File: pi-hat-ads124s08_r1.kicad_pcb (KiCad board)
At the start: 4 copper layers, 65 x 56 mm, 65 parts, among them J1 GPIO, J2 Conn_01x06, J3 Conn_01x06, J4 Conn_01x06, J5 Conn_01x06, J6 Conn_01x04, J7 Conn_01x02, Q1 S8550, U1 M24c64, U2 HX711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

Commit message: blocking out...
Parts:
- removed C2: 100nF, Capacitor_SMD:C_0603_1608Metric
- removed Q1: S8550, Package_TO_SOT_SMD:SOT-23
- removed R11, R13: 10k, Resistor_SMD:R_0603_1608Metric
- removed R12, R15, R20: 0R, Resistor_SMD:R_0603_1608Metric
- removed R14: 3k9, Resistor_SMD:R_0603_1608Metric
- removed R16, R17: 100R, Resistor_SMD:R_0603_1608Metric
- removed TP1: TestPoint, TestPoint:TestPoint_THTPad_2.0x2.0mm_Drill1.0mm
- added C17: 10nF, Capacitor_SMD:C_0603_1608Metric, F.Cu at (119.6, 80.7)
- C3: value 10uF -> 100nF; footprint Capacitor_SMD:C_0805_2012Metric -> Capacitor_SMD:C_0603_1608Metric
- C4: value 100nF -> 1uF
- C5: value 100nF -> 220nF
- C9: value 33pF -> 220nF
- J6: value Conn_01x04 -> Conn_01x06; footprint Connector_PinHeader_2.54mm:PinHeader_1x04_P2.54mm_Vertical -> Connector_PinHeader_2.54mm:PinHeader_1x06_P2.54mm_Vertical
- R10, R9: value 0R -> 1k
- R2, R4: value 100R -> 10k
- U2: value HX711 -> ADS124S08; footprint Package_SO:SOIC-16_3.9x9.9mm_P1.27mm -> Package_QFP:TQFP-32_5x5mm_P0.5mm
- moved J7 55.8 mm to (161.0, 71.9), turned to 90 degrees
- moved R9 23.9 mm to (146.5, 83.7), turned to 90 degrees
- moved R10 23.2 mm to (144.0, 83.8), turned to 90 degrees
- moved J4 23.0 mm to (135.8, 96.6), turned to 0 degrees
- moved R8 22.2 mm to (145.8, 56.0), turned to -90 degrees
- moved J6 19.7 mm to (132.2, 38.2), turned to 180 degrees
- moved C9 19.4 mm to (123.0, 73.0), turned to -90 degrees
- moved D2 18.0 mm to (155.8, 87.2), turned to 0 degrees
- moved C3 14.7 mm to (135.8, 71.7)
- moved J3 13.3 mm to (151.6, 87.2), turned to -90 degrees
- moved R4 11.4 mm to (118.1, 83.5), turned to 90 degrees
- moved D3 11.3 mm to (130.2, 87.2)
- moved J5 11.3 mm to (125.9, 87.2)
- moved J2 11.2 mm to (110.1, 96.6)
- moved R2 11.2 mm to (120.8, 83.5), turned to 90 degrees
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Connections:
- C3 pad 1: /EXE1+ -> +3V3
- C4 pad 1: /EXE1+ -> Net-(U2C-REFOUT)
- C5 pad 1: Net-(U2-VBG) -> VDDA
- C9 pad 1: Net-(U2-XI) -> VDDA
- C9 pad 2: /GPIO13/PWM1 -> GND
- D2 pad 2: GND -> /EXE1-
- D3 pad 1: /EXE1+ -> /EXE2+
- D3 pad 2: GND -> /EXE2-
- J2 pad 1: GND -> /EXE1-
- J3 pad 1: /EXE1+ -> /EXE2+
- J3 pad 6: GND -> /EXE2-
- J4 pad 1: GND -> /EXE2-
- J4 pad 6: /EXE1+ -> /EXE2+
- J5 pad 6: GND -> /EXE1-
- J6 pad 1: /GPIO8/SPI0.CE0 -> unconnected-(J6-Pin_1-Pad1)
- J6 pad 2: /GPIO9/SPI0.MISO -> /GPIO10/SPI0.MOSI
- J6 pad 4: /GPIO13/PWM1 -> /GPIO9/SPI0.MISO
- R10 pad 1: /EXE1+ -> /BR_OUT2-
- R10 pad 2: Net-(Q1-E) -> /Analog/INB-
- R2 pad 1: /Analog/IN1+ -> /BR_OUT1+
- R2 pad 2: /BR_OUT1+ -> /Analog/INA+
- R4 pad 1: /Analog/IN1- -> /BR_OUT1-
- R4 pad 2: /BR_OUT1- -> /Analog/INA-
- R8 pad 1: Net-(Q1-B) -> GND
- R8 pad 2: Net-(U2-BASE) -> /GPIO13/PWM1
- R9 pad 1: Net-(Q1-E) -> /BR_OUT2+
- R9 pad 2: VDDA -> /Analog/INB+
- U2 pad 1: VDDA -> unconnected-(U2A-AINCOM-Pad1)
- U2 pad 10: /Analog/INB+ -> /GPIO10/SPI0.MOSI
- U2 pad 13: unconnected-(U2-XO-Pad13) -> /GPIO17
- U2 pad 14: Net-(U2-XI) -> GND
- U2 pad 15: Net-(U2-RATE) -> +3V3
- U2 pad 2: Net-(U2-BASE) -> unconnected-(U2A-AIN5-Pad2)
- U2 pad 3: /EXE1+ -> unconnected-(U2A-AIN4-Pad3)
- U2 pad 4: Net-(U2-VFB) -> /Analog/INA-
- U2 pad 5: GND -> /Analog/INA+
- U2 pad 6: Net-(U2-VBG) -> /Analog/INB-
- U2 pad 7: /Analog/IN1- -> /Analog/INB+
- U2 pad 8: /Analog/IN1+ -> /GPIO5
- U2 pad 9: /Analog/INB- -> /GPIO8/SPI0.CE0
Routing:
- net /EXE1+: track 108.2 -> 21.0 mm, vias 5 -> 0
- net /GPIO10/SPI0.MOSI: track 0.00 -> 37.1 mm
- net +5V: track 70.9 -> 46.7 mm
- net +3V3: track 66.3 -> 47.5 mm, vias 3 -> 2
- net /GPIO8/SPI0.CE0: track 28.7 -> 45.0 mm
- net /power/VBOOST: track 39.8 -> 24.4 mm
- net /GPIO13/PWM1: track 23.5 -> 10.6 mm, vias 1 -> 0
- net Net-(U2-VFB): track 11.0 -> 0.00 mm
- net /GPIO11/SPI0.SCLK: track 38.5 -> 29.3 mm
- net /Analog/IN1-: track 8.66 -> 0.00 mm
- net VDDA: track 27.1 -> 18.9 mm
- net Net-(U2-VBG): track 7.76 -> 0.00 mm
- net /BR_OUT2-: track 16.3 -> 8.87 mm
- net /BR_OUT2+: track 16.0 -> 9.08 mm
- net Net-(U2-XI): track 6.70 -> 0.00 mm
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- removed copper zone on F.Cu, net /EXE1+
- removed copper zone on In2.Cu, net /EXE1+
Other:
- outline, holes or cut-outs redrawn
- board text removed: "CAMERA (OPTIONAL)"
- board text removed: "EX+"
- board text removed: "VDDA Mode R8<->R10 R20<->R15"

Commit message: progressing, blocking things out, pondering orbz
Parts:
- moved J6 27.9 mm to (136.4, 65.8), turned to 90 degrees
- moved R8 14.0 mm to (133.3, 62.4), turned to 90 degrees
- moved C10 1.00 mm to (145.2, 82.0)
- moved C17 1.00 mm to (119.6, 81.7)
- moved D2 1.00 mm to (155.8, 88.2)
- moved D3 1.00 mm to (130.2, 88.2)
- moved J3 1.00 mm to (151.6, 88.2)
- moved J5 1.00 mm to (125.9, 88.2)
- moved R10 1.00 mm to (144.0, 84.8)
- moved R2 1.00 mm to (120.8, 84.5)
- moved R4 1.00 mm to (118.1, 84.5)
- moved R9 1.00 mm to (146.5, 84.7)
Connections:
- J6 pad 1: unconnected-(J6-Pin_1-Pad1) -> /GPIO24
- J6 pad 2: /GPIO10/SPI0.MOSI -> /GPIO9/SPI0.MISO
- J6 pad 4: /GPIO9/SPI0.MISO -> /GPIO10/SPI0.MOSI
- J6 pad 6: unconnected-(J6-Pin_6-Pad6) -> /GPIO5
- R8 pad 2: /GPIO13/PWM1 -> /GPIO18/PCM.CLK
- U2 pad 13: /GPIO17 -> /GPIO24
- U2 pad 17: /GPIO13/PWM1 -> /GPIO18/PCM.CLK
- U2 pad 18: /GPIO6 -> /GPIO22
- U2 pad 2: unconnected-(U2A-AIN5-Pad2) -> /Analog/INA-
- U2 pad 3: unconnected-(U2A-AIN4-Pad3) -> /Analog/INA+
- U2 pad 4: /Analog/INA- -> unconnected-(U2A-AIN3-Pad4)
- U2 pad 5: /Analog/INA+ -> unconnected-(U2A-AIN2-Pad5)
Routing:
- net /GPIO5: track 0.00 -> 44.6 mm
- net /GPIO24: track 0.00 -> 36.1 mm
- net /GPIO18/PCM.CLK: track 0.00 -> 31.9 mm, vias 0 -> 1
- net /REFIN2+: track 7.60 -> 36.2 mm, vias 0 -> 1
- net /GPIO22: track 0.00 -> 25.5 mm, vias 0 -> 1
- net /REFIN2-: track 7.58 -> 30.9 mm, vias 0 -> 1
- net +5V: track 46.7 -> 23.9 mm
- net /REFIN1-: track 10.2 -> 30.8 mm
- net /REFIN1+: track 10.3 -> 27.7 mm, vias 0 -> 1
- net /Analog/INB+: track 0.00 -> 16.4 mm
- net /Analog/INB-: track 0.00 -> 15.7 mm
- net /Analog/INA-: track 0.00 -> 11.8 mm
- net /Analog/INA+: track 0.00 -> 11.0 mm
- net /GPIO13/PWM1: track 10.6 -> 0.00 mm
- net /GPIO9/SPI0.MISO: track 41.5 -> 32.7 mm
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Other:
- board text added: "ADS124S08-IIO-Eval karlp@tweak.au rev2025.10"
- board text added: "DRDY MISO CLK MOSI START"
- board text removed: "HX711-IIO-Eval karlp@tweak.au rev2025.09"
- board text removed: "Rate DO CLK XI"

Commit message: overhausl inputs a lot
read too much, thought too much.
try one with the "just 0R plus a nice big good quality cap" from the TI
precision seminar, describing common realities, as well as mixing in
what they did on the ads1262ref scale design document for the second
channel with a more "full blown" input filter.

I don't really like how none of this seems to be a proper AA filter,
but... ok.
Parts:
- added R11: 22R, Resistor_SMD:R_0603_1608Metric, F.Cu at (163.4, 103.7)
- added R12: 22R, Resistor_SMD:R_0603_1608Metric, F.Cu at (160.8, 103.7)
- added R13: 22R, Resistor_SMD:R_0603_1608Metric, F.Cu at (158.3, 103.7)
- added R14: 22R, Resistor_SMD:R_0603_1608Metric, F.Cu at (155.8, 103.7)
- added R15: 22R, Resistor_SMD:R_0603_1608Metric, F.Cu at (153.3, 103.7)
- added R16: 22R, Resistor_SMD:R_0603_1608Metric, F.Cu at (150.8, 103.7)
- added R17: 22R, Resistor_SMD:R_0603_1608Metric, F.Cu at (148.3, 103.7)
- added REF**: R_Array_Concave_4x0603, Resistor_SMD:R_Array_Concave_4x0603, F.Cu at (124.1, 84.5)
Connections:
- R8 pad 2: /GPIO18/PCM.CLK -> /Analog/EXT_CLK
- U2 pad 10: /GPIO10/SPI0.MOSI -> /Analog/SPI_MOSI
- U2 pad 11: /GPIO11/SPI0.SCLK -> /Analog/SPI_CLK
- U2 pad 12: /GPIO9/SPI0.MISO -> /Analog/SPI_MISO
- U2 pad 13: /GPIO24 -> /Analog/~{ADC_READY}
- U2 pad 17: /GPIO18/PCM.CLK -> /Analog/EXT_CLK
- U2 pad 8: /GPIO5 -> /Analog/ADC_START
- U2 pad 9: /GPIO8/SPI0.CE0 -> /Analog/SPI_CS

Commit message: thanks, I hate it.
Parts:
- removed R10, R9: 1k, Resistor_SMD:R_0603_1608Metric
- removed REF**: R_Array_Concave_4x0603, Resistor_SMD:R_Array_Concave_4x0603
- added C18: 220nF, Capacitor_SMD:C_1206_3216Metric, F.Cu at (116.8, 78.9)
- added C19: 100pF, Capacitor_SMD:C_0603_1608Metric, F.Cu at (132.2, 81.9)
- added C2: 220nF, Capacitor_SMD:C_1206_3216Metric, F.Cu at (134.2, 83.5)
- added C20: 1uF, jlc-extras:C_Feedthrough_NFM21_2.0mmx1.2mm, F.Cu at (146.3, 81.0)
- added C21: 1uF, jlc-extras:C_Feedthrough_NFM21_2.0mmx1.2mm, F.Cu at (144.2, 81.0)
- added C22: 1uF, jlc-extras:C_Feedthrough_NFM21_2.0mmx1.2mm, F.Cu at (137.4, 85.0)
- added C23: 1uF, jlc-extras:C_Feedthrough_NFM21_2.0mmx1.2mm, F.Cu at (137.4, 82.2)
- added C24: 100pF, Capacitor_SMD:C_0603_1608Metric, F.Cu at (132.2, 85.0)
- added C25: 100pF, Capacitor_SMD:C_0603_1608Metric, F.Cu at (139.3, 79.8)
- added C26: 100pF, Capacitor_SMD:C_0603_1608Metric, F.Cu at (139.3, 78.3)
- added C27: 1uF, Capacitor_SMD:C_0603_1608Metric, F.Cu at (129.6, 86.0)
- added C28: 1uF, Capacitor_SMD:C_0603_1608Metric, F.Cu at (155.1, 86.2)
- added R22: 0R, Resistor_SMD:R_0603_1608Metric, F.Cu at (116.9, 82.1)
- added R23: 0R, Resistor_SMD:R_0603_1608Metric, F.Cu at (115.3, 82.1)
- added RN1: 47R, Resistor_SMD:R_Array_Convex_4x0603, F.Cu at (145.3, 84.2)
- C10: value 100nF -> 220nF; footprint Capacitor_SMD:C_0603_1608Metric -> Capacitor_SMD:C_1206_3216Metric
- C17: value 10nF -> 220nF; footprint Capacitor_SMD:C_0603_1608Metric -> Capacitor_SMD:C_1206_3216Metric
- J6: value Conn_01x06 -> Conn_02x04_Odd_Even; footprint Connector_PinHeader_2.54mm:PinHeader_1x06_P2.54mm_Vertical -> Connector_PinHeader_2.54mm:PinHeader_2x04_P2.54mm_Vertical
- R2, R4: value 10k -> 0R
- moved R11 46.0 mm to (141.6, 63.1)
- moved R12 43.7 mm to (139.1, 65.8)
- moved R15 43.4 mm to (139.1, 62.7)
- moved R13 43.0 mm to (144.5, 63.0)
- moved R17 42.9 mm to (134.3, 63.1)
- moved R14 39.8 mm to (141.8, 66.4)
- moved R16 37.4 mm to (144.5, 66.8)
- moved J6 7.53 mm to (136.3, 58.3)
- moved R8 4.17 mm to (134.3, 66.4)
- moved C10 3.93 mm to (142.0, 79.6), turned to -90 degrees
- moved R4 1.79 mm to (119.9, 84.7)
- moved C17 1.75 mm to (121.4, 81.8)
- moved X1 1.63 mm to (109.6, 74.7)
- moved R2 1.53 mm to (122.3, 84.5)
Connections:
- D2 pad 2: /EXE1- -> GND
- D3 pad 2: /EXE2- -> GND
- J2 pad 1: /EXE1- -> GND
- J3 pad 6: /EXE2- -> GND
- J4 pad 1: /EXE2- -> GND
- J5 pad 6: /EXE1- -> GND
- J6 pad 1: /GPIO24 -> /GPIO18/PCM.CLK
- J6 pad 2: /GPIO9/SPI0.MISO -> /GPIO22
- J6 pad 3: /GPIO11/SPI0.SCLK -> /GPIO24
- J6 pad 4: /GPIO10/SPI0.MOSI -> /GPIO9/SPI0.MISO
- J6 pad 5: /GPIO8/SPI0.CE0 -> /GPIO11/SPI0.SCLK
- J6 pad 6: /GPIO5 -> /GPIO10/SPI0.MOSI
- U2 pad 29: /REFIN1- -> /Analog/SENSEA-
- U2 pad 30: /REFIN1+ -> /Analog/SENSEA+
- U2 pad 31: /REFIN2- -> /Analog/SENSEB-
- U2 pad 32: /REFIN2+ -> /Analog/SENSEB+
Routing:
- net /GPIO5: track 44.6 -> 18.1 mm
- net /GPIO8/SPI0.CE0: track 45.1 -> 19.3 mm
- net /Analog/ADC_START: track 0.00 -> 22.3 mm
- net /REFIN2+: track 36.2 -> 14.0 mm, vias 1 -> 0
- net /Analog/SPI_CS: track 0.00 -> 21.8 mm
- net /REFIN2-: track 30.9 -> 9.23 mm, vias 1 -> 0
- net /REFIN1-: track 30.8 -> 10.2 mm
- net /GPIO10/SPI0.MOSI: track 44.8 -> 24.5 mm
- net /GPIO11/SPI0.SCLK: track 34.4 -> 15.7 mm
- net /REFIN1+: track 27.7 -> 10.5 mm
- net /Analog/SPI_CLK: track 0.00 -> 17.0 mm
- net /Analog/SPI_MOSI: track 0.00 -> 15.2 mm
- net /GPIO24: track 36.1 -> 21.1 mm
- net /Analog/~{ADC_READY}: track 0.00 -> 14.2 mm
- net /Analog/SENSEA-: track 0.00 -> 13.6 mm
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
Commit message: moarh updates
we commit to save our progress
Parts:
- added C29: 10nF, Capacitor_SMD:C_0603_1608Metric, F.Cu at (150.3, 71.2)
- added D4: LED_0805_Yellow, LED_SMD:LED_0805_2012Metric, F.Cu at (125.7, 55.5)
- added D5: LED_0805_Red, LED_SMD:LED_0805_2012Metric, F.Cu at (127.7, 55.5)
- added D6: LED_0805_Green, LED_SMD:LED_0805_2012Metric, F.Cu at (129.7, 55.5)
- added J10: Conn_01x02, Connector_Phoenix_MC:PhoenixContact_MCV_1,5_2-G-3.81_1x02_P3.81mm_Vertical, F.Cu at (161.5, 73.2)
- added J11: Conn_01x02, Connector_Phoenix_MC:PhoenixContact_MCV_1,5_2-G-3.81_1x02_P3.81mm_Vertical, F.Cu at (161.5, 83.3)
- added J9: Conn_01x03, Connector_PinHeader_2.54mm:PinHeader_1x03_P2.54mm_Vertical, F.Cu at (130.7, 61.9)
- added R10: 1k, Resistor_SMD:R_0603_1608Metric, F.Cu at (129.7, 58.8)
- added R20: 1k, Resistor_SMD:R_0603_1608Metric, F.Cu at (125.7, 58.8)
- added R21: 5k1, Resistor_SMD:R_0603_1608Metric, F.Cu at (153.2, 69.4)
- added R24: 5k1, Resistor_SMD:R_0603_1608Metric, F.Cu at (153.2, 73.2)
- added R25: 0R, Resistor_SMD:R_0603_1608Metric, F.Cu at (109.0, 85.1)
- added R9: 1k, Resistor_SMD:R_0603_1608Metric, F.Cu at (127.7, 58.8)
- JP1, JP3: footprint Jumper:SolderJumper-2_P1.3mm_Open_TrianglePad1.0x1.5mm -> jlc-extras:SolderJumper-2_P1.3mm_Open_TrianglePad0.9x1.8mm
- U2: footprint Package_QFP:TQFP-32_5x5mm_P0.5mm -> Package_QFP:LQFP-32_5x5mm_P0.5mm
- moved X1 39.7 mm to (149.0, 79.9)
- moved TP5 31.2 mm to (103.7, 52.6), turned to 180 degrees
- moved TP4 28.6 mm to (103.7, 55.1), turned to 180 degrees
- moved TP2 26.7 mm to (103.7, 57.7), turned to 180 degrees
- moved D3 25.7 mm to (155.8, 88.2)
- moved D2 25.7 mm to (130.1, 88.2)
- moved TP3 23.7 mm to (103.7, 60.2), turned to 180 degrees
- moved J7 8.79 mm to (161.5, 63.1)
- moved C21 7.87 mm to (136.3, 80.5)
- moved C24 7.21 mm to (129.8, 78.2), turned to 90 degrees
- moved C20 7.07 mm to (139.3, 80.5)
- moved C22 6.50 mm to (132.6, 80.6)
- moved C25 5.89 mm to (133.8, 77.7)
- moved C19 5.57 mm to (126.9, 83.6), turned to 180 degrees
- moved C28 5.51 mm to (158.1, 90.8)
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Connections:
- C20 pad 1: Net-(RN1-R3.2) -> Net-(RN1-R4.2)
- C21 pad 3: Net-(RN1-R2.2) -> Net-(RN1-R3.2)
- C22 pad 1: Net-(RN1-R4.2) -> Net-(RN1-R2.2)
- C28 pad 1: /EXE2+ -> /EXE1+
- D3 pad 1: /EXE2+ -> /EXE1+
- J3 pad 1: /EXE2+ -> /EXE1+
- J4 pad 6: /EXE2+ -> /EXE1+
- RN1 pad 2: /BR_OUT2- -> /REFIN2+
- RN1 pad 3: /BR_OUT2+ -> /BR_OUT2-
- RN1 pad 4: /REFIN2+ -> /BR_OUT2+
- U2 pad 1: unconnected-(U2A-AINCOM-Pad1) -> /Analog/AINCOM
- U2 pad 19: unconnected-(U2A-GPIO3/AIN11-Pad19) -> Net-(J9-Pin_1)
- U2 pad 20: unconnected-(U2A-GPIO2/AIN10-Pad20) -> Net-(J9-Pin_2)
- U2 pad 21: unconnected-(U2A-GPIO1/AIN9-Pad21) -> Net-(J9-Pin_3)
- U2 pad 4: unconnected-(U2A-AIN3-Pad4) -> /Analog/INB-
- U2 pad 5: unconnected-(U2A-AIN2-Pad5) -> /Analog/INB+
- U2 pad 6: /Analog/INB- -> /Analog/INC-
- U2 pad 7: /Analog/INB+ -> /Analog/INC+
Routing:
- net /EXE1+: track 21.0 -> 97.1 mm, vias 0 -> 1
- net +5V: track 23.9 -> 76.7 mm
- net /Analog/AINCOM: track 0.00 -> 37.9 mm, vias 0 -> 1
- net VDDA: track 18.9 -> 55.7 mm, vias 1 -> 4
- net +3V3: track 47.5 -> 71.5 mm, vias 2 -> 3
- net /Analog/INC-: track 0.00 -> 23.7 mm
- net /Analog/INC+: track 0.00 -> 23.3 mm
- net /Analog/SENSEB-: track 4.72 -> 19.8 mm, vias 1 -> 2
- net /Analog/SENSEB+: track 3.99 -> 17.4 mm, vias 1 -> 2
- net /Analog/INB+: track 3.22 -> 14.4 mm
- net Net-(J9-Pin_3): track 0.00 -> 10.0 mm
- net /Analog/INB-: track 4.36 -> 14.1 mm
- net Net-(J9-Pin_2): track 0.00 -> 8.57 mm
- net Net-(RN1-R2.2): track 0.00 -> 8.43 mm
- net /REFIN1+: track 10.5 -> 18.9 mm
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- added copper zone on F.Cu, net +3V3
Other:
- board text added: "EXC+/AICOM"
- board text added: "IN3-/IN3+"

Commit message: "ready" ?
Added 0805 footprints for the diff caps, to try different values there.
for the smaller nF values, 080 is _way_ cheaper than the 1206 that's
~required for the big nF values.

Pushed a lot of silk....
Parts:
- added C30: C_Small, Capacitor_SMD:C_0805_2012Metric, F.Cu at (121.6, 78.9)
- added C31: C_Small, Capacitor_SMD:C_0805_2012Metric, F.Cu at (116.8, 78.9)
- added C32: C_Small, Capacitor_SMD:C_0805_2012Metric, F.Cu at (137.8, 76.0)
- added C33: C_Small, Capacitor_SMD:C_0805_2012Metric, F.Cu at (127.4, 81.0)
- C20, C21, C22, C23: value 1uF -> 100nF
- moved J9 4.99 mm to (125.9, 60.6), turned to 90 degrees
- moved R18 3.75 mm to (121.4, 51.4), turned to 0 degrees
- moved C17 2.24 mm to (121.6, 81.1)
- moved C18 2.24 mm to (116.8, 81.1)
- moved R2 2.24 mm to (123.1, 83.9)
- moved R22 2.24 mm to (118.2, 83.9)
- moved R23 2.24 mm to (115.3, 83.9)
- moved R4 2.24 mm to (120.1, 83.9)
- moved R19 2.23 mm to (124.5, 51.4), turned to 0 degrees
- moved C15 2.09 mm to (122.3, 54.0)
- moved U3 2.00 mm to (119.4, 54.0)
- moved D4 1.60 mm to (125.9, 54.0)
- moved D6 1.60 mm to (129.9, 54.0)
- moved R10 1.60 mm to (129.9, 57.2)
- moved R20 1.60 mm to (125.9, 57.2)
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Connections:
- net Net-(J9-Pin_2) renamed /Analog/G2
- J9 pad 1: Net-(J9-Pin_1) -> /Analog/G1
- J9 pad 3: Net-(J9-Pin_3) -> /Analog/G3
- R10 pad 2: Net-(J9-Pin_1) -> /Analog/G3
- R20 pad 2: Net-(J9-Pin_3) -> /Analog/G1
- U2 pad 19: Net-(J9-Pin_1) -> /Analog/G3
- U2 pad 21: Net-(J9-Pin_3) -> /Analog/G1
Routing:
- net /Analog/G1: track 0.00 -> 11.0 mm
- net Net-(J9-Pin_3): track 10.0 -> 0.00 mm
- net /Analog/G3: track 0.00 -> 9.13 mm
- net Net-(J9-Pin_1): track 7.66 -> 0.00 mm
- net /Analog/SENSEA-: track 19.0 -> 23.0 mm
- net /Analog/SENSEA+: track 18.2 -> 22.0 mm
- net /Analog/SENSEB+: track 17.4 -> 20.2 mm
- net /Analog/INA+: track 15.2 -> 17.8 mm
- net /Analog/INA-: track 15.2 -> 17.8 mm
- net +3V3: track 71.5 -> 73.9 mm
- net /REFIN1+: track 18.9 -> 16.5 mm
- net /BR_OUT1+: track 16.4 -> 14.1 mm
- net /BR_OUT1-: track 16.1 -> 13.9 mm
- net /Analog/INB+: track 14.4 -> 16.1 mm
- net /Analog/INB-: track 14.1 -> 15.5 mm
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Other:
- board text added: "EXP-ADS124S08-IIO karlp@tweak.au rev2025.10"
- board text added: "G1|G2|G3"
- board text added: "Hat-ADS124S08-IIO karlp@tweak.au rev2025.10"
- board text removed: "ADS124S08-IIO-Eval karlp@tweak.au rev2025.10"

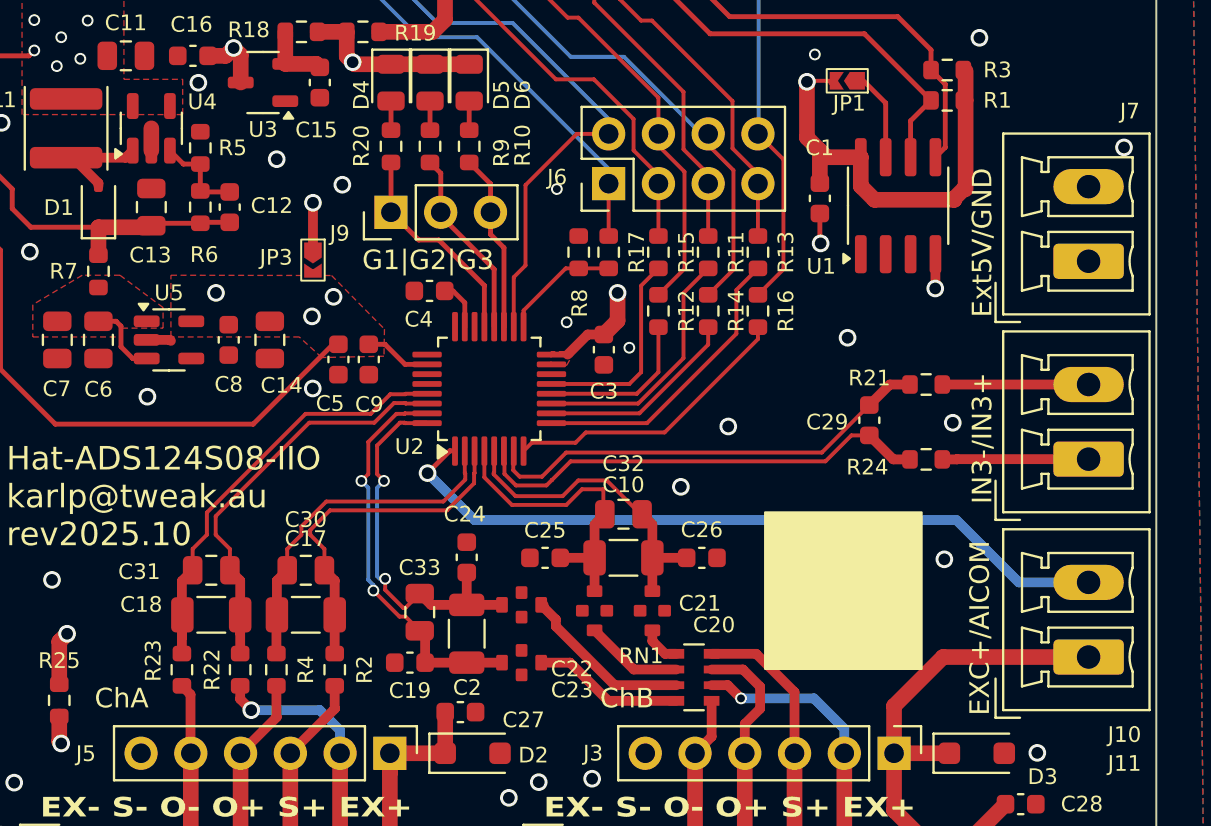
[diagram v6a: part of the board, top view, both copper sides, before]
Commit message: "final" to order
added a jumper for aincom to ground.
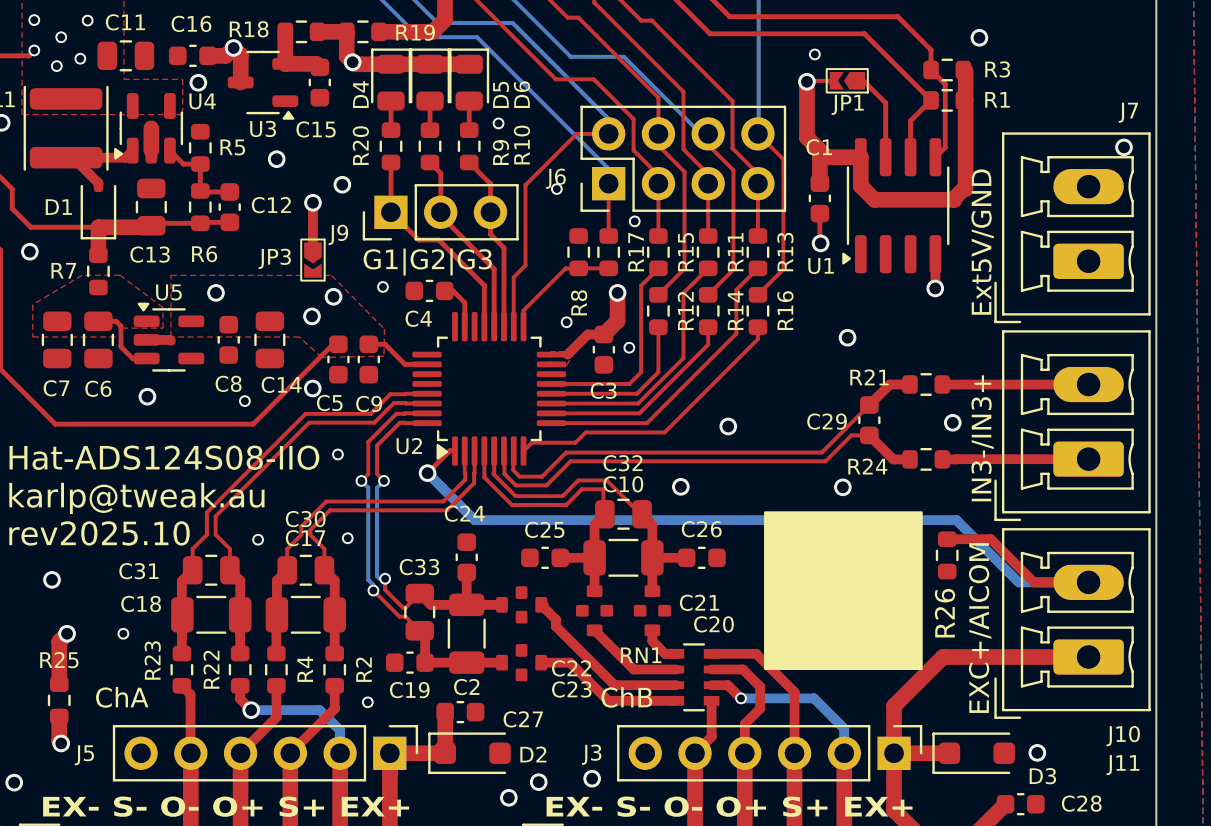
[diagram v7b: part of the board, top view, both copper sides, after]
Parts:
- added R26: 0R, Resistor_SMD:R_0603_1608Metric, F.Cu at (154.3, 78.1)
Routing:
- net /Analog/AINCOM: track 37.9 -> 46.1 mm
- net GND: vias 29 -> 38
